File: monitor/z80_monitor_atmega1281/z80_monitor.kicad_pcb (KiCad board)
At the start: 2 copper layers, 2 parts, among them J1 Conn_02x25_Odd_Even, U1 ATmega1281-16AU

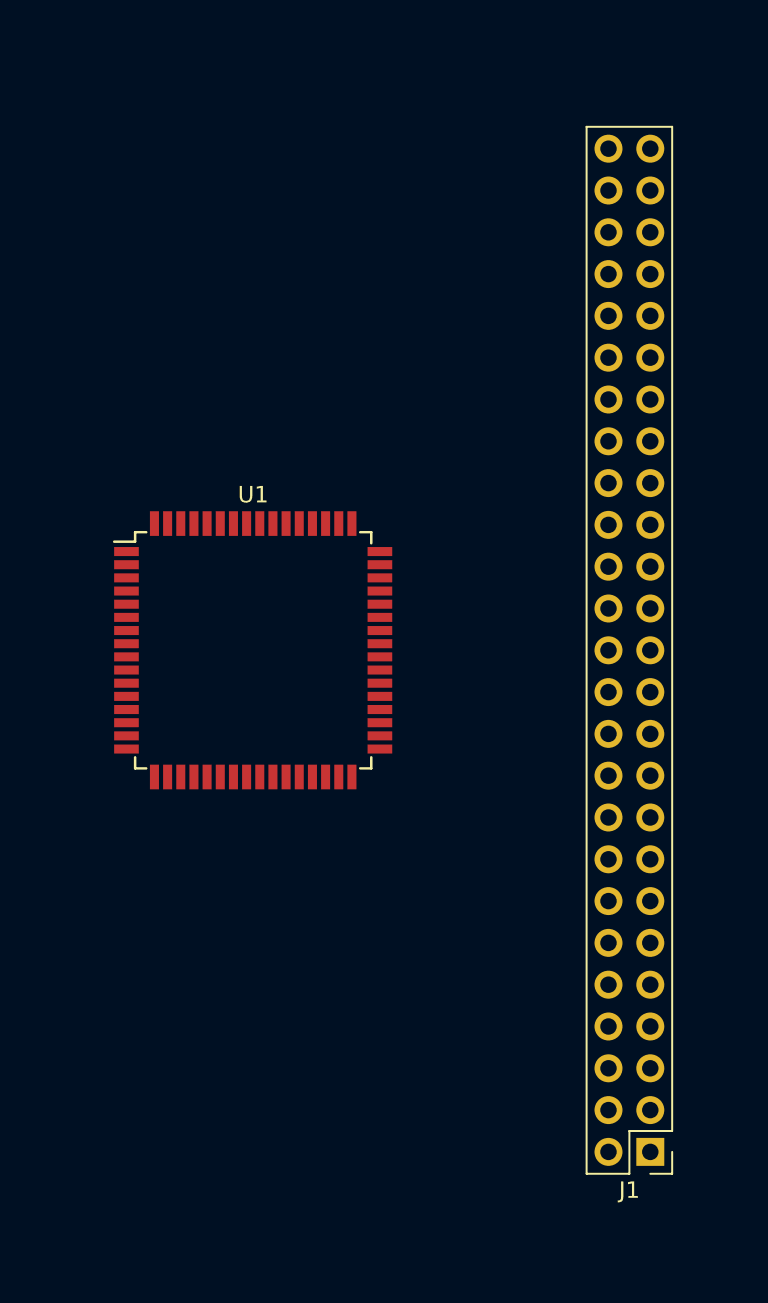
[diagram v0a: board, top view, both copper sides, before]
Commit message: Finished new AVR-based monitor board, pending final checks and gerber generation.
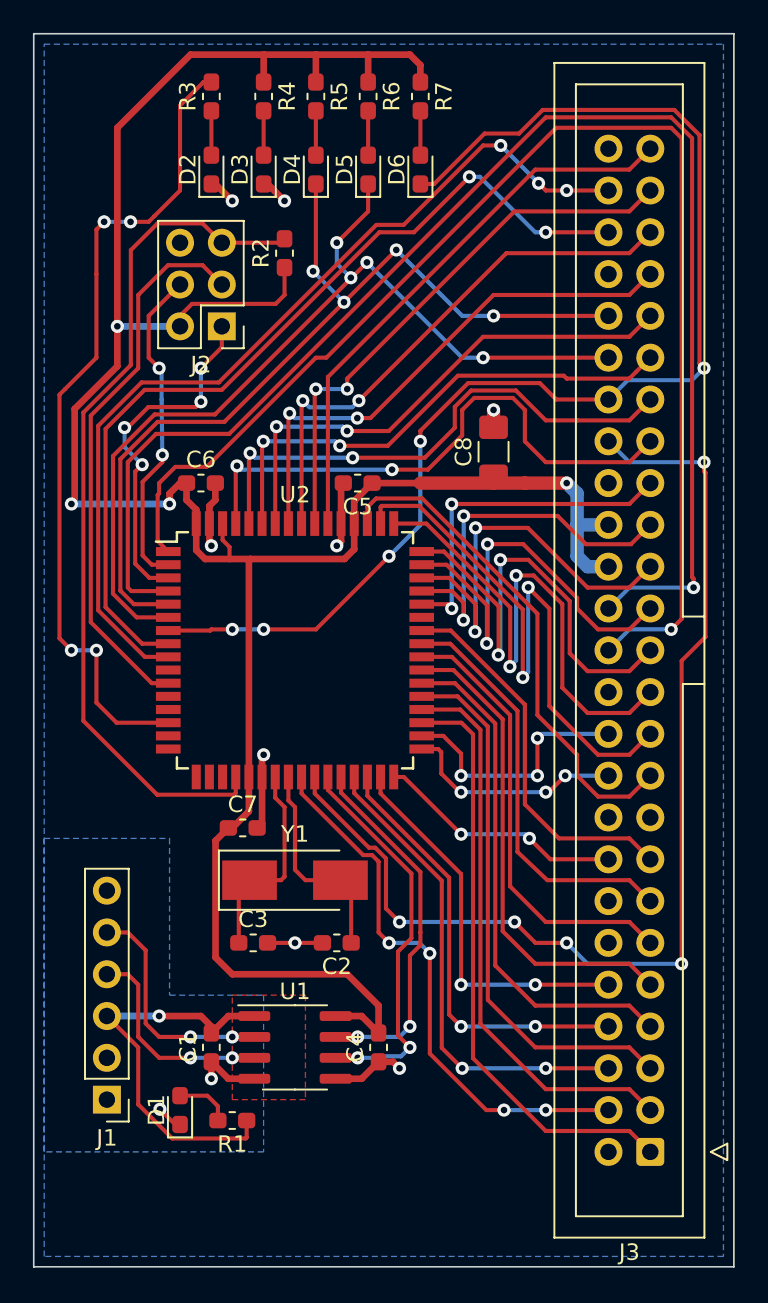
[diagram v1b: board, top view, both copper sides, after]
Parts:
- added C1: 0u1, Capacitor_SMD:C_0603_1608Metric_Pad1.05x0.95mm_HandSolder, F.Cu at (204.5, 105.4)
- added C2: 15p, Capacitor_SMD:C_0603_1608Metric_Pad1.05x0.95mm_HandSolder, F.Cu at (212.1, 99.1)
- added C3: 15p, Capacitor_SMD:C_0603_1608Metric_Pad1.05x0.95mm_HandSolder, F.Cu at (207.0, 99.1)
- added C4: 0u1, Capacitor_SMD:C_0603_1608Metric_Pad1.05x0.95mm_HandSolder, F.Cu at (214.6, 105.4)
- added C5: 0u1, Capacitor_SMD:C_0603_1608Metric_Pad1.05x0.95mm_HandSolder, F.Cu at (213.4, 71.1)
- added C6: 0u1, Capacitor_SMD:C_0603_1608Metric_Pad1.05x0.95mm_HandSolder, F.Cu at (203.8, 71.1)
- added C7: 0u1, Capacitor_SMD:C_0603_1608Metric_Pad1.05x0.95mm_HandSolder, F.Cu at (206.4, 92.1)
- added C8: 10u, Capacitor_SMD:C_1206_3216Metric_Pad1.42x1.75mm_HandSolder, F.Cu at (221.6, 69.2)
- added D1: GRN, LED_SMD:LED_0603_1608Metric_Pad1.05x0.95mm_HandSolder, F.Cu at (202.6, 109.2)
- added D2: YEL, LED_SMD:LED_0603_1608Metric_Pad1.05x0.95mm_HandSolder, F.Cu at (204.5, 52.1)
- added D3: GRN, LED_SMD:LED_0603_1608Metric_Pad1.05x0.95mm_HandSolder, F.Cu at (207.6, 52.1)
- added D4: BLU, LED_SMD:LED_0603_1608Metric_Pad1.05x0.95mm_HandSolder, F.Cu at (210.8, 52.1)
- added D5: BLU, LED_SMD:LED_0603_1608Metric_Pad1.05x0.95mm_HandSolder, F.Cu at (214.0, 52.1)
- added D6: RED, LED_SMD:LED_0603_1608Metric_Pad1.05x0.95mm_HandSolder, F.Cu at (217.2, 52.1)
- added J1: Conn_01x06, Connector_PinHeader_2.54mm:PinHeader_1x06_P2.54mm_Vertical, F.Cu at (198.1, 108.6)
- added J2: Conn_02x03_Odd_Even, Connector_PinHeader_2.54mm:PinHeader_2x03_P2.54mm_Vertical, F.Cu at (205.1, 61.6)
- added R1: 1K0, Resistor_SMD:R_0603_1608Metric_Pad1.05x0.95mm_HandSolder, F.Cu at (205.7, 109.9)
- added R2: 10K, Resistor_SMD:R_0603_1608Metric_Pad1.05x0.95mm_HandSolder, F.Cu at (208.9, 57.1)
- added R3: 1K0, Resistor_SMD:R_0603_1608Metric_Pad1.05x0.95mm_HandSolder, F.Cu at (204.5, 47.6)
- added R4: 1K0, Resistor_SMD:R_0603_1608Metric_Pad1.05x0.95mm_HandSolder, F.Cu at (207.6, 47.6)
- added R5: 1K0, Resistor_SMD:R_0603_1608Metric_Pad1.05x0.95mm_HandSolder, F.Cu at (210.8, 47.6)
- added R6: 1K0, Resistor_SMD:R_0603_1608Metric_Pad1.05x0.95mm_HandSolder, F.Cu at (214.0, 47.6)
- added R7: 1K0, Resistor_SMD:R_0603_1608Metric_Pad1.05x0.95mm_HandSolder, F.Cu at (217.2, 47.6)
- added U1: ADuM1201CR, Package_SO:SOIC-8_3.9x4.9mm_P1.27mm, F.Cu at (209.6, 105.4)
- added Y1: 16MHz, Crystal:Crystal_SMD_Abracon_ABM3-2Pin_5.0x3.2mm_HandSoldering, F.Cu at (209.6, 95.2)
- J3: renamed from J1; footprint Pin_Headers:Pin_Header_Straight_2x25_Pitch2.54mm -> Connector_IDC:IDC-Header_2x25_P2.54mm_Vertical
- moved U2 2.54 mm to (209.6, 81.3)
- renumbered U1 to U2
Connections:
- J3 pad 30: /TARGET_PWR -> +5V
- J3 pad 32: /TARGET_PWR -> +5V
- U2 pad 1: Net-(U1-Pad1) -> /~NMI~
- U2 pad 11: Net-(U1-Pad11) -> /SCK
- U2 pad 2: Net-(U1-Pad2) -> /PDI
- U2 pad 20: Net-(U1-Pad20) -> /~RST~
- U2 pad 21: Net-(U1-Pad21) -> +5V
- U2 pad 22: Net-(U1-Pad22) -> GND
- U2 pad 25: Net-(U1-Pad25) -> /~IORQ~
- U2 pad 26: Net-(U1-Pad26) -> /~MREQ~
- U2 pad 27: Net-(U1-Pad27) -> /RXD1
- U2 pad 28: Net-(U1-Pad28) -> /TXD1
- U2 pad 29: Net-(U1-Pad29) -> /~RD~
- U2 pad 3: Net-(U1-Pad3) -> /PDO
- U2 pad 30: Net-(U1-Pad30) -> /~WR~
- U2 pad 31: Net-(U1-Pad31) -> /~M1~
- U2 pad 32: Net-(U1-Pad32) -> /~RESET~
- U2 pad 33: Net-(U1-Pad33) -> /~WAIT~
- U2 pad 34: Net-(U1-Pad34) -> /~INT~
- U2 pad 4: Net-(U1-Pad4) -> /RSVD0
- U2 pad 5: Net-(U1-Pad5) -> /~BUSRQ~
- U2 pad 52: Net-(U1-Pad21) -> +5V
- U2 pad 53: Net-(U1-Pad22) -> GND
- U2 pad 6: Net-(U1-Pad6) -> /~BUSAK~
- U2 pad 62: Net-(U1-Pad62) -> +5V
- U2 pad 63: Net-(U1-Pad22) -> GND
- U2 pad 64: Net-(U1-Pad64) -> +5V
- U2 pad 7: Net-(U1-Pad7) -> /~HALT~
- U2 pad 8: Net-(U1-Pad8) -> /RSVD1
- U2 pad 9: Net-(U1-Pad9) -> /RSVD2
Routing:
- net +5V: track 0.00 -> 154.7 mm, vias 0 -> 4
- net /RSVD0: track 0.00 -> 86.7 mm, vias 0 -> 1
- net /~NMI~: track 0.00 -> 79.9 mm, vias 0 -> 1
- net /~HALT~: track 0.00 -> 77.1 mm, vias 0 -> 5
- net /~MREQ~: track 0.00 -> 66.8 mm, vias 0 -> 5
- net /~BUSAK~: track 0.00 -> 56.5 mm, vias 0 -> 4
- net /~BUSRQ~: track 0.00 -> 55.9 mm, vias 0 -> 4
- net /RSVD2: track 0.00 -> 55.8 mm, vias 0 -> 3
- net /RSVD1: track 0.00 -> 53.9 mm, vias 0 -> 2
- net /~RST~: track 0.00 -> 52.5 mm
- net Net-(R3-Pad2): track 0.00 -> 50.1 mm, vias 0 -> 4
- net /A1: track 0.00 -> 37.6 mm, vias 0 -> 2
- net /D0: track 0.00 -> 36.2 mm
- net /A8: track 0.00 -> 34.7 mm, vias 0 -> 2
- net /D1: track 0.00 -> 34.4 mm
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- added copper zone on B.Cu, net /ISO_GND
- added copper zone on F.Cu, net /ISO_GND
- added copper zone on B.Cu, net GND
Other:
- board outline added: 42.5 x 74.9 mm
- net class 16mil added: clearance 0.2, trace_width 0.4064, via_dia 0.9, via_drill 0.5
- net class 32mil added: clearance 0.2, trace_width 0.8128, via_dia 0.8, via_drill 0.4

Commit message: Move LEDs to edge of board and label. Add 2x M2.5 clearance hole.
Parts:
- added REF**: MountingHole_2.7mm_M2.5, MountingHole:MountingHole_2.7mm_M2.5, F.Cu at (130.2, 121.9)
- added REF**: MountingHole_2.7mm_M2.5, MountingHole:MountingHole_2.7mm_M2.5, F.Cu at (130.2, 55.9)
- moved R3 99.2 mm to (106.0, 59.7), turned to 270 degrees
- moved D2 98.5 mm to (106.0, 55.9), turned to 270 degrees
- moved R4 97.3 mm to (111.1, 59.7), turned to 90 degrees
- moved D3 96.6 mm to (111.1, 55.9), turned to 270 degrees
- moved R5 95.4 mm to (116.2, 59.7), turned to 90 degrees
- moved D4 94.7 mm to (116.2, 55.9), turned to 270 degrees
- moved R6 93.5 mm to (121.3, 59.7), turned to 90 degrees
- moved D5 92.8 mm to (121.3, 55.9), turned to 270 degrees
- moved R7 92.2 mm to (125.7, 59.7), turned to 90 degrees
- moved C5 91.8 mm to (121.9, 78.7)
- moved C6 91.8 mm to (112.4, 78.7)
- moved R1 91.8 mm to (114.3, 117.5)
- moved U1 91.8 mm to (118.1, 113.0)
- moved U2 91.8 mm to (118.1, 88.9)
- moved Y1 91.8 mm to (118.1, 102.9)
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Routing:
- net Net-(R3-Pad2): track 50.1 -> 39.1 mm, vias 4 -> 2
- net /~BUSRQ~: track 55.9 -> 63.8 mm
- net +5V: track 154.7 -> 147.0 mm, vias 4 -> 6
- net /~BUSAK~: track 56.5 -> 62.7 mm
- net /~HALT~: track 77.1 -> 81.9 mm
- net /RSVD1: track 53.9 -> 51.5 mm
- net /RSVD2: track 55.8 -> 53.9 mm, vias 3 -> 2
- net /~NMI~: track 79.9 -> 80.6 mm
- net /RSVD0: track 86.7 -> 87.4 mm
- net Net-(D6-Pad2): track 2.70 -> 2.06 mm
- net Net-(D5-Pad2): track 2.70 -> 2.06 mm
- net Net-(D4-Pad2): track 2.70 -> 2.06 mm
- net Net-(D3-Pad2): track 2.70 -> 2.06 mm
- net Net-(D2-Pad2): track 2.70 -> 2.06 mm
- net GND: track 24.8 -> 24.3 mm
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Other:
- board text added: "ACK"
- board text added: "COMS"
- board text added: "HALT"
- board text added: "PWR"
- board text added: "REQ"
- board text added: "Z80 Monitor R1 J.L.Macfarlane 2020"

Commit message: Various updates to board.
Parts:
- removed the C3 at (115.6, 106.7)
- removed the C5 at (121.9, 78.7)
- removed REF** (x2): MountingHole_2.7mm_M2.5, MountingHole:MountingHole_2.7mm_M2.5
- added C2: 100p, Capacitor_SMD:C_0603_1608Metric_Pad1.05x0.95mm_HandSolder, F.Cu at (118.7, 117.5)
- added C4: 15p, Capacitor_SMD:C_0603_1608Metric_Pad1.05x0.95mm_HandSolder, F.Cu at (115.6, 106.7)
- added C6: 0u1, Capacitor_SMD:C_0603_1608Metric_Pad1.05x0.95mm_HandSolder, F.Cu at (121.9, 78.7)
- added H1: M2.5, MountingHole:MountingHole_2.7mm_M2.5_Pad_Via, F.Cu at (130.2, 55.9)
- added H2: MountingHole_Pad, MountingHole:MountingHole_2.7mm_M2.5_Pad_Via, F.Cu at (130.2, 121.9)
- moved D2 5.08 mm to (111.1, 55.9)
- moved D3 5.08 mm to (106.0, 55.9)
- moved R3 5.08 mm to (111.1, 59.7)
- moved R4 5.08 mm to (106.0, 59.7)
- renumbered C2 to C3, C4 to C5, C6 to C7, C7 to C8, C8 to C9
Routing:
- net /~HALT~: track 81.9 -> 86.3 mm, vias 5 -> 7
- net Net-(R3-Pad2): track 39.1 -> 42.0 mm, vias 2 -> 0
- net +5V: track 147.0 -> 149.4 mm, vias 6 -> 8
- net /~RST~: track 52.5 -> 50.6 mm, vias 0 -> 2
- net /ISO_GND: track 5.66 -> 7.33 mm
- net GND: track 24.3 -> 25.3 mm, vias 8 -> 9
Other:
- outline, holes or cut-outs redrawn
